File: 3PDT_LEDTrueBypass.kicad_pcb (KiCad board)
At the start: 2 copper layers, 25.7 x 17.1 mm, 9 parts, among them J1 G, J2 S, J3 O, J4 I, J5 R, J6 +9V, SW1 SW_3PDT

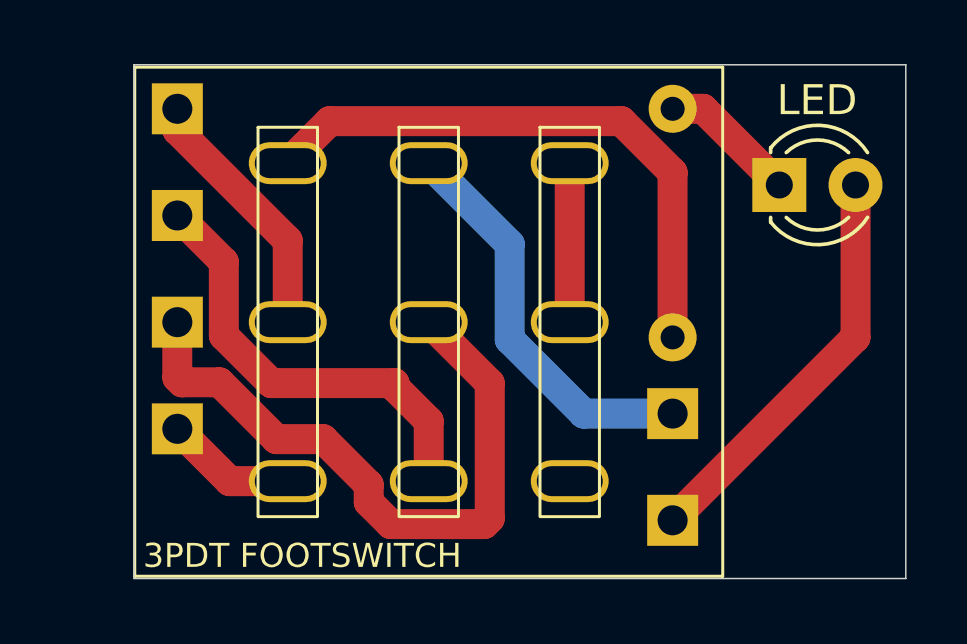
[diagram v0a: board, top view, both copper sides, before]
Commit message: overhauled, rerouted and fixed pin spacings - vertical and horizontal spacings were mixed up
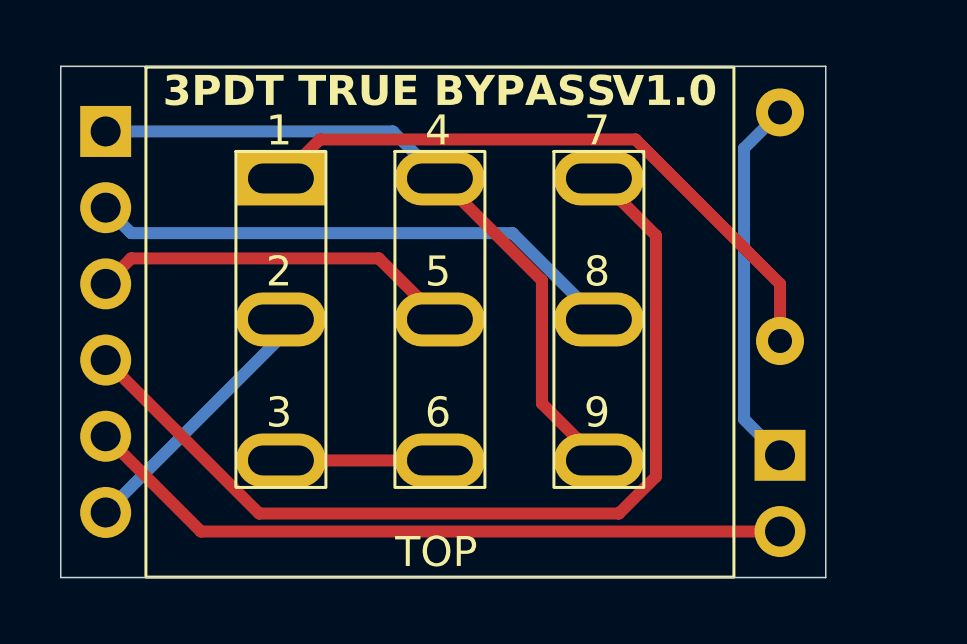
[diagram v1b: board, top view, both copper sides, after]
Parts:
- removed J1: G, Connector_PinSocket_2.54mm:PinSocket_1x01_P2.54mm_Vertical
- removed J2: S, Connector_PinSocket_2.54mm:PinSocket_1x01_P2.54mm_Vertical
- removed J3: O, Connector_PinSocket_2.54mm:PinSocket_1x01_P2.54mm_Vertical
- removed J4: I, Connector_PinSocket_2.54mm:PinSocket_1x01_P2.54mm_Vertical
- removed J5: R, Connector_PinSocket_2.54mm:PinSocket_1x01_P2.54mm_Vertical
- removed J6: +9V, Connector_PinSocket_2.54mm:PinSocket_1x01_P2.54mm_Vertical
- added J7: Conn_01x06_Pin, Connector_PinHeader_2.54mm:PinHeader_1x06_P2.54mm_Vertical, B.Cu at (65.6, 49.7)
- D1: footprint LED_THT:LED_D3.0mm -> Connector_PinHeader_2.54mm:PinHeader_1x02_P2.54mm_Vertical; moved to B.Cu
- moved D1 9.01 mm to (88.1, 60.5), turned to 180 degrees
- moved R1 3.58 mm to (88.1, 56.7)
- moved SW1 0.37 mm to (76.8, 55.6)
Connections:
- SW1 pad 4: Net-(J4-Pin_1) -> Net-(J7-Input)
- SW1 pad 9: unconnected-(SW1-I-Pad9) -> Net-(J7-Input)
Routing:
- net Net-(J7-Effects_Return): track 4.40 -> 31.7 mm
- net Net-(J7-Input): track 0.00 -> 23.4 mm
- net Net-(D1-A): track 13.7 -> 23.8 mm
- net Net-(J7-Effects_Send): track 22.1 -> 12.3 mm
- net Net-(J4-Pin_1): track 8.64 -> 0.00 mm
- net Net-(D1-K): track 4.61 -> 12.4 mm
- net Net-(J7-GND): track 13.5 -> 8.85 mm
- net Net-(J7-Output): track 14.7 -> 18.0 mm
- net Net-(SW1-A): track 19.6 -> 21.1 mm
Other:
- board size 25.7 x 17.1 mm -> 25.5 x 17 mm
- board text added: "+"
- board text added: "+9V"
- board text added: "-"
- board text added: "BOTTOM"
- board text added: "GND"
- board text added: "IN"
- board text added: "OUT"
- board text added: "RTN"
- board text added: "SND"
- board text added: "TOP"
- board text added: "github.com/fablabnk/ SynthLabProjects"
- board text removed: "3PDT FOOTSWITCH"
